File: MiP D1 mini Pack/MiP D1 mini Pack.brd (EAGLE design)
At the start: 41.4 x 63.8 mm, 6 parts, among them J2 D1 mini, J3 Debug

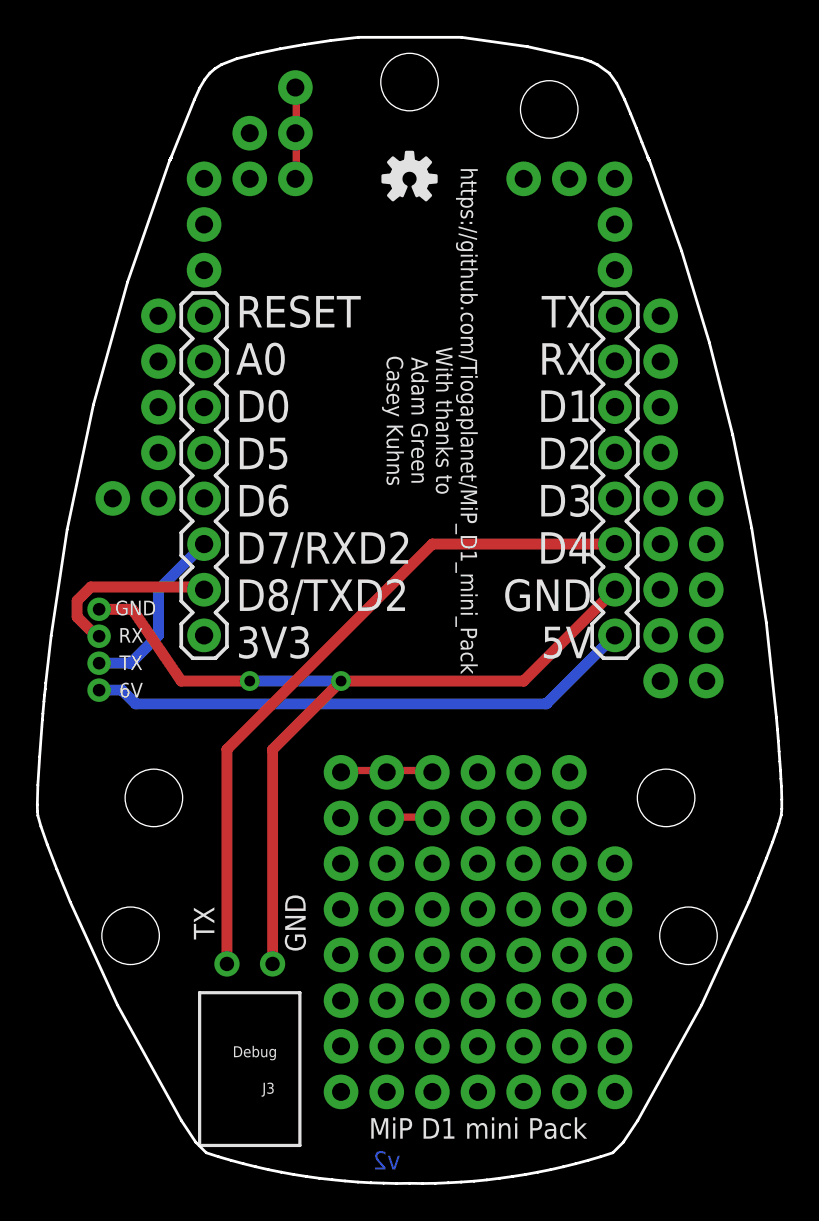
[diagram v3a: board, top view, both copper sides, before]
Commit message: Deleted more connected vias
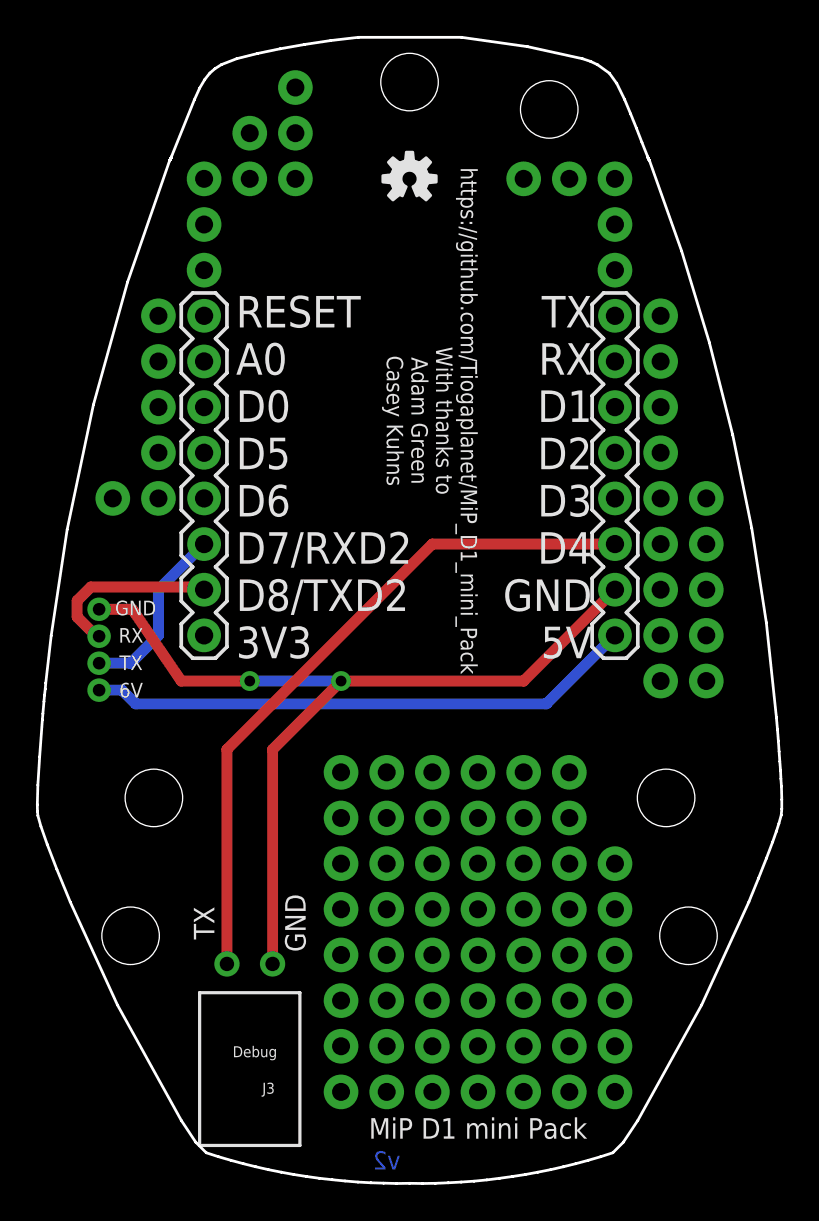
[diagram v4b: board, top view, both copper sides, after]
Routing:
- net N$30: track 5.30 -> 0.00 mm, vias 3 -> 0
- net N$1: track 5.18 -> 0.00 mm, vias 3 -> 1
- net N$96: track 2.60 -> 0.00 mm, vias 2 -> 0
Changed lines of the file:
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@@
 <via x="35.56" y="19.05" extent="1-16" drill="1" diameter="1.9304"/>
-</signal>
-<signal name="N$30">
-<via x="25.4" y="24.13" extent="1-16" drill="1" diameter="1.9304"/>
-<via x="22.86" y="24.13" extent="1-16" drill="1" diameter="1.9304"/>
-<via x="20.32" y="24.13" extent="1-16" drill="1" diameter="1.9304"/>
-<wire x1="22.86" y1="24.2316" x2="20.4216" y2="24.2316" width="0.4064" layer="1"/>
-<wire x1="20.4216" y1="24.2316" x2="20.32" y2="24.13" width="0.4064" layer="1"/>
-<wire x1="22.86" y1="24.2316" x2="22.86" y2="24.13" width="0.4064" layer="1"/>
-<wire x1="25.2984" y1="24.2316" x2="23.0124" y2="24.2316" width="0.4064" layer="1"/>
-<wire x1="23.0124" y1="24.2316" x2="22.86" y2="24.13" width="0.4064" layer="1"/>
-<wire x1="25.2984" y1="24.2316" x2="25.4" y2="24.13" width="0.4064" layer="1"/>
 </signal>
 <signal name="N$32">
@@
 <via x="10.16" y="49.53" extent="1-16" drill="1" diameter="1.9304"/>
 </signal>
-<signal name="N$96">
+<signal name="N$39">
 <via x="25.4" y="21.59" extent="1-16" drill="1" diameter="1.9304"/>
-<via x="22.86" y="21.59" extent="1-16" drill="1" diameter="1.9304"/>
-<wire x1="25.2984" y1="21.6408" x2="22.86" y2="21.6408" width="0.4064" layer="1"/>
-<wire x1="22.86" y1="21.6408" x2="22.86" y2="21.59" width="0.4064" layer="1"/>
-<wire x1="25.2984" y1="21.6408" x2="25.4" y2="21.59" width="0.4064" layer="1"/>
 </signal>
 <signal name="N$98">
@@
 <via x="12.7" y="57.15" extent="1-16" drill="1" diameter="1.9304"/>
 </signal>
+<signal name="N$24">
+<via x="17.78" y="62.23" extent="1-16" drill="1" diameter="1.9304"/>
+</signal>
+<signal name="N$25">
+<via x="17.78" y="57.15" extent="1-16" drill="1" diameter="1.9304"/>
+</signal>
 <signal name="N$1">
-<via x="17.78" y="57.15" extent="1-16" drill="1" diameter="1.9304"/>
 <via x="17.78" y="59.69" extent="1-16" drill="1" diameter="1.9304"/>
-<via x="17.78" y="62.23" extent="1-16" drill="1" diameter="1.9304"/>
-<wire x1="17.8308" y1="59.5884" x2="17.8308" y2="57.15" width="0.4064" layer="1"/>
-<wire x1="17.8308" y1="57.15" x2="17.78" y2="57.15" width="0.4064" layer="1"/>
-<wire x1="17.8308" y1="59.5884" x2="17.78" y2="59.69" width="0.4064" layer="1"/>
-<wire x1="17.8308" y1="62.1792" x2="17.8308" y2="59.7408" width="0.4064" layer="1"/>
-<wire x1="17.8308" y1="59.7408" x2="17.78" y2="59.69" width="0.4064" layer="1"/>
-<wire x1="17.8308" y1="62.1792" x2="17.78" y2="62.23" width="0.4064" layer="1"/>
 </signal>
 <signal name="N$4">
@@
 <signal name="N$11">
 <via x="20.32" y="21.59" extent="1-16" drill="1" diameter="1.9304"/>
+<via x="20.32" y="24.13" extent="1-16" drill="1" diameter="1.9304"/>
+<via x="22.86" y="24.13" extent="1-16" drill="1" diameter="1.9304"/>
+<via x="22.86" y="21.59" extent="1-16" drill="1" diameter="1.9304"/>
+<via x="25.4" y="24.13" extent="1-16" drill="1" diameter="1.9304"/>
 </signal>
 <signal name="N$12">
